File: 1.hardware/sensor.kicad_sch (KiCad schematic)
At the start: 13 parts, among them U10 Hall_Analog_Joystick, U2 LM75B, U9 Hall_Analog_Joystick

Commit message: 중간 저장
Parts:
- added C79, C80, C84, C88: 39nF/16V, symbol Device:C_Small_US
- added R125, R129, R2, R3: 100/0.1w, Resistor_SMD:R_0402_1005Metric, symbol Device:R_Small_US
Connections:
- net GND: now also C79.2, C80.2, C84.2, C88.2
- net Joystick1_H: now also C84.1, R125.1; no longer TP32.1, U9.2 (H)
- net Joystick1_V: now also C88.1, R129.2; no longer TP33.1, U9.5 (V)
- net Joystick2_H: now also C80.1, R3.1; no longer TP35.1, U10.2 (H)
- net Joystick2_V: now also C79.1, R2.2; no longer TP34.1, U10.5 (V)
- new net: R3.2, TP35.1, U10.2 (H)
- new net: R125.2, TP32.1, U9.2 (H)
- new net: R2.1, TP34.1, U10.5 (V)
- new net: R129.1, TP33.1, U9.5 (V)
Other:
- moved on the sheet: C67, R108, R109, R112, R113, R114, TP32, TP33, TP34, TP35, U10, U2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

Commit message: 핀 배치 완료
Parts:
- removed R113, R114: 10k/0.063w, Resistor_SMD:R_0402_1005Metric, symbol Device:R_Small_US
- removed U2: LM75B, symbol Sensor_Temperature:LM75B
- added RT1: NCP18XH103F03RB, THRMC1608X95N, symbol SamacSys_Parts:NCP18XH103F03RB
- R112: footprint Resistor_SMD:R_0402_1005Metric -> (none)
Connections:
- net +3.3V: no longer C67.1, R112.1
- net GND: now also R112.1
- net ADC_TEMP: now reaches R112.2
- net ADC_TEMP: now also C67.1, RT1.1
- new net ADC_VREF_2V5: RT1.2
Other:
- note removed: "TEMP"

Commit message: 중간 저장
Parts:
- C80: value 39nF/16V -> 39nF/50V; footprint (none) -> Capacitor_SMD:C_0402_1005Metric
- C81: renamed from C84; value 39nF/16V -> 39nF/50V; footprint (none) -> Capacitor_SMD:C_0402_1005Metric
- C82: renamed from C88; value 39nF/16V -> 39nF/50V; footprint (none) -> Capacitor_SMD:C_0402_1005Metric
- C83: renamed from C79; value 39nF/16V -> 39nF/50V; footprint (none) -> Capacitor_SMD:C_0402_1005Metric
- R131: renamed from R112; footprint (none) -> Resistor_SMD:R_0402_1005Metric
- R132: renamed from R3; footprint Resistor_SMD:R_0402_1005Metric -> Resistor_SMD:R_0603_1608Metric
- R133: renamed from R125; footprint Resistor_SMD:R_0402_1005Metric -> Resistor_SMD:R_0603_1608Metric
- R136: renamed from R129; footprint Resistor_SMD:R_0402_1005Metric -> Resistor_SMD:R_0603_1608Metric
- R137: renamed from R2; footprint Resistor_SMD:R_0402_1005Metric -> Resistor_SMD:R_0603_1608Metric
- TP10: renamed from TP33; footprint (none) -> TestPoint:TestPoint_Pad_D1.5mm
- TP11: renamed from TP34; footprint (none) -> TestPoint:TestPoint_Pad_D1.5mm
- TP8: renamed from TP35; footprint (none) -> TestPoint:TestPoint_Pad_D1.5mm
- TP9: renamed from TP32; footprint (none) -> TestPoint:TestPoint_Pad_D1.5mm
- renumbered C67 to C79, R108 to R134, R109 to R135, U9 to U7, U10 to U8

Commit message: 풋프린트 연결 완료
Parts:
- RT1: footprint THRMC1608X95N -> SamacSys_Parts_Project:THRMC1608X95N
- U7, U8: footprint New_Footprints:Hall_Analog_Joystick -> Library:Hall_Analog_Joystick
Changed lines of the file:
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@@
 			)
 		)
-		(property "Footprint" "New_Footprints:Hall_Analog_Joystick"
+		(property "Footprint" "Library:Hall_Analog_Joystick"
 			(at 95.25 120.65 0)
 			(effects
@@
 			)
 		)
-		(property "Footprint" "THRMC1608X95N"
+		(property "Footprint" "SamacSys_Parts_Project:THRMC1608X95N"
 			(at 55.88 175.26 0)
 			(effects
@@
 			)
 		)
-		(property "Footprint" "New_Footprints:Hall_Analog_Joystick"
+		(property "Footprint" "Library:Hall_Analog_Joystick"
 			(at 95.25 73.66 0)
 			(effects

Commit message: 중간 저장
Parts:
- removed C80, C83: 39nF/50V, Capacitor_SMD:C_0402_1005Metric, symbol Device:C_Small_US
- removed R132, R137: 100/0.1w, Resistor_SMD:R_0603_1608Metric, symbol Device:R_Small_US
- removed R135: 4.7k/0.063w, Resistor_SMD:R_0402_1005Metric, symbol Device:R_Small_US
- removed TP11: TP_JV2, TestPoint:TestPoint_Pad_D1.5mm, symbol Connector:TestPoint
- removed TP8: TP_JH2, TestPoint:TestPoint_Pad_D1.5mm, symbol Connector:TestPoint
- removed U8: Hall_Analog_Joystick, Library:Hall_Analog_Joystick, symbol New_Library:Hall_Analog_Sensor
- renumbered C79 to C81, C81 to C82, C82 to C83, R131 to R119, R133 to R120, R134 to R121, R136 to R122, TP9 to TP8, TP10 to TP9, U7 to U8
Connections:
- net Joystick1_H renamed Joystick_H
- net Joystick1_Sel renamed Joystick_Sel
- net Joystick1_V renamed Joystick_V

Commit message: 중간 저장
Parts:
- renumbered C82 to C81, C83 to C82, C81 to C83, R120 to R115, R122 to R116, R121 to R117, R119 to R118, TP8 to TP7, TP9 to TP8, U8 to U22
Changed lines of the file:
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@@
 		(dnp no)
 		(fields_autoplaced yes)
-		(property "Reference" "#PWR0121"
+		(property "Reference" "#PWR0114"
 			(at 102.87 95.25 0)
 			(effects
@@
 			(project "bldc_motor_controller"
 				(path "/a25adab6-a8c3-4e0e-8ba9-baac00aaa394/41a95291-f7f2-4bdf-b0a1-cf2084f10036"
-					(reference "#PWR0121")
+					(reference "#PWR0114")
 					(unit 1)
 				)
@@
 		(dnp no)
 		(fields_autoplaced yes)
-		(property "Reference" "#PWR0120"
+		(property "Reference" "#PWR0115"
 			(at 93.98 100.33 0)
 			(effects
@@
 			(project "bldc_motor_controller"
 				(path "/a25adab6-a8c3-4e0e-8ba9-baac00aaa394/41a95291-f7f2-4bdf-b0a1-cf2084f10036"
-					(reference "#PWR0120")
+					(reference "#PWR0115")
 					(unit 1)
 				)
@@
 		(on_board yes)
 		(dnp no)
-		(property "Reference" "R119"
+		(property "Reference" "R118"
 			(at 54.102 194.818 0)
 			(effects
@@
 			(project "bldc_motor_controller"
 				(path "/a25adab6-a8c3-4e0e-8ba9-baac00aaa394/41a95291-f7f2-4bdf-b0a1-cf2084f10036"
-					(reference "R119")
+					(reference "R118")
 					(unit 1)
 				)
@@
 		(dnp no)
 		(fields_autoplaced yes)
-		(property "Reference" "#PWR0119"
+		(property "Reference" "#PWR0112"
 			(at 60.96 90.17 0)
 			(effects
@@
 			(project "bldc_motor_controller"
 				(path "/a25adab6-a8c3-4e0e-8ba9-baac00aaa394/41a95291-f7f2-4bdf-b0a1-cf2084f10036"
-					(reference "#PWR0119")
+					(reference "#PWR0112")
 					(unit 1)
 				)
@@
 		(on_board yes)
 		(dnp no)
-		(property "Reference" "R120"
+		(property "Reference" "R115"
 			(at 65.532 71.374 90)
 			(effects
@@
 			(project "bldc_motor_controller"
 				(path "/a25adab6-a8c3-4e0e-8ba9-baac00aaa394/41a95291-f7f2-4bdf-b0a1-cf2084f10036"
-					(reference "R120")
+					(reference "R115")
 					(unit 1)
 				)
@@
 		(dnp no)
 		(fields_autoplaced yes)
-		(property "Reference" "#PWR0117"
+		(property "Reference" "#PWR0116"
 			(at 48.26 208.28 0)
 			(effects
@@
 			(project "bldc_motor_controller"
 				(path "/a25adab6-a8c3-4e0e-8ba9-baac00aaa394/41a95291-f7f2-4bdf-b0a1-cf2084f10036"
-					(reference "#PWR0117")
+					(reference "#PWR0116")
 					(unit 1)
 				)
@@
 		(on_board yes)
 		(dnp no)
-		(property "Reference" "TP8"
+		(property "Reference" "TP7"
 			(at 69.85 65.786 0)
 			(effects
@@
 			(project "bldc_motor_controller"
 				(path "/a25adab6-a8c3-4e0e-8ba9-baac00aaa394/41a95291-f7f2-4bdf-b0a1-cf2084f10036"
-					(reference "TP8")
+					(reference "TP7")
 					(unit 1)
 				)
@@
 		(on_board yes)
 		(dnp no)
-		(property "Reference" "C82"
+		(property "Reference" "C81"
 			(at 63.5 77.5969 0)
 			(effects
@@
 			(project "bldc_motor_controller"
 				(path "/a25adab6-a8c3-4e0e-8ba9-baac00aaa394/41a95291-f7f2-4bdf-b0a1-cf2084f10036"
-					(reference "C82")
+					(reference "C81")
 					(unit 1)
 				)
@@
 		(dnp no)
 		(fields_autoplaced yes)
-		(property "Reference" "#PWR0118"
+		(property "Reference" "#PWR0117"
 			(at 57.15 208.28 0)
 			(effects
@@
 			(project "bldc_motor_controller"
 				(path "/a25adab6-a8c3-4e0e-8ba9-baac00aaa394/41a95291-f7f2-4bdf-b0a1-cf2084f10036"
-					(reference "#PWR0118")
+					(reference "#PWR0117")
 					(unit 1)
 				)
@@
 		(dnp no)
 		(fields_autoplaced yes)
-		(property "Reference" "U8"
+		(property "Reference" "U22"
 			(at 95.885 62.23 0)
 			(effects
@@
 			(project ""
 				(path "/a25adab6-a8c3-4e0e-8ba9-baac00aaa394/41a95291-f7f2-4bdf-b0a1-cf2084f10036"
-					(reference "U8")
+					(reference "U22")
 					(unit 1)
 				)
@@
 		(on_board yes)
 		(dnp no)
-		(property "Reference" "R121"
+		(property "Reference" "R117"
 			(at 103.124 93.98 0)
 			(effects
@@
 			(project "bldc_motor_controller"
 				(path "/a25adab6-a8c3-4e0e-8ba9-baac00aaa394/41a95291-f7f2-4bdf-b0a1-cf2084f10036"
-					(reference "R121")
+					(reference "R117")
 					(unit 1)
 				)
@@
 		(on_board yes)
 		(dnp no)
-		(property "Reference" "C81"
+		(property "Reference" "C83"
 			(at 44.196 196.342 0)
 			(effects
@@
 			(project "bldc_motor_controller"
 				(path "/a25adab6-a8c3-4e0e-8ba9-baac00aaa394/41a95291-f7f2-4bdf-b0a1-cf2084f10036"
-					(reference "C81")
+					(reference "C83")
 					(unit 1)
 				)
@@
 		(dnp no)
 		(fields_autoplaced yes)
-		(property "Reference" "#PWR0122"
+		(property "Reference" "#PWR0113"
 			(at 130.81 90.17 0)
 			(effects
@@
 			(project "bldc_motor_controller"
 				(path "/a25adab6-a8c3-4e0e-8ba9-baac00aaa394/41a95291-f7f2-4bdf-b0a1-cf2084f10036"
-					(reference "#PWR0122")
+					(reference "#PWR0113")
 					(unit 1)
 				)
@@
 		(on_board yes)
 		(dnp no)
-		(property "Reference" "TP9"
+		(property "Reference" "TP8"
 			(at 115.57 65.278 0)
 			(effects
@@
 			(project "bldc_motor_controller"
 				(path "/a25adab6-a8c3-4e0e-8ba9-baac00aaa394/41a95291-f7f2-4bdf-b0a1-cf2084f10036"
-					(reference "TP9")
+					(reference "TP8")
 					(unit 1)
 				)
@@
 		(on_board yes)
 		(dnp no)
-		(property "Reference" "C83"
+		(property "Reference" "C82"
 			(at 133.35 77.5969 0)
 			(effects
@@
 			(project "bldc_motor_controller"
 				(path "/a25adab6-a8c3-4e0e-8ba9-baac00aaa394/41a95291-f7f2-4bdf-b0a1-cf2084f10036"
-					(reference "C83")
+					(reference "C82")
 					(unit 1)
 				)
@@
 		(on_board yes)
 		(dnp no)
-		(property "Reference" "R122"
+		(property "Reference" "R116"
 			(at 122.682 71.374 90)
 			(effects
@@
 			(project "bldc_motor_controller"
 				(path "/a25adab6-a8c3-4e0e-8ba9-baac00aaa394/41a95291-f7f2-4bdf-b0a1-cf2084f10036"
-					(reference "R122")
-					(unit 1)
-				)
+					(reference "R116")
+					(unit 1)
+				)

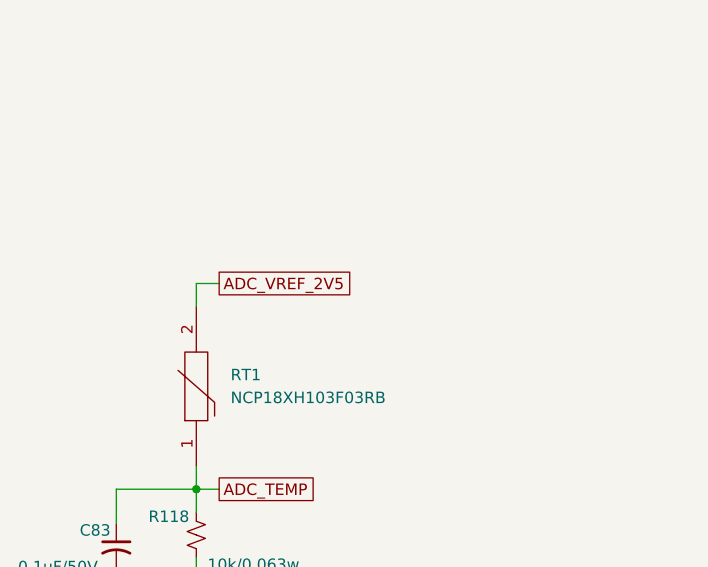
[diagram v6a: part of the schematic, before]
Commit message: 스펙 정함
4층 기판, 비아 0.3 / 0.5 사이즈, 외부 2온즈, Plugger Via, 77달러 정도 나옴
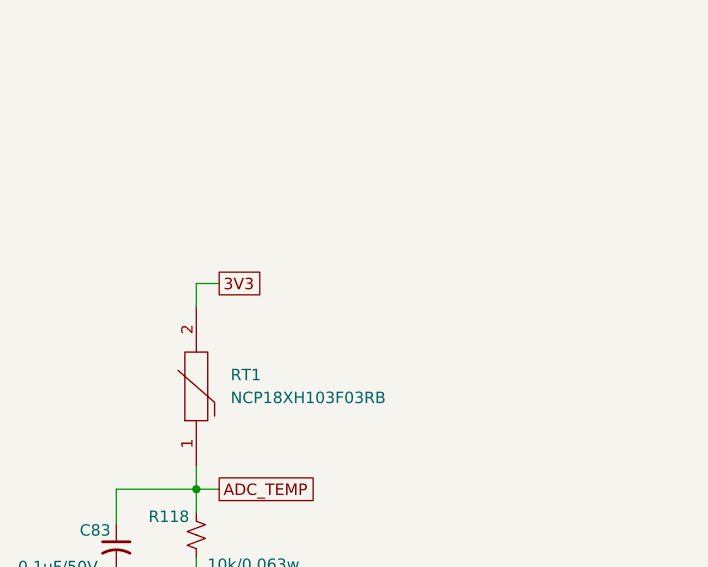
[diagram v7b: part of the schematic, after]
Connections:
- net ADC_VREF_2V5 renamed 3V3
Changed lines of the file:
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@@
 		)
 	)
-	(global_label "ADC_VREF_2V5"
+	(global_label "3V3"
 		(shape passive)
 		(at 59.69 168.91 0)
@@
 		)
 		(property "Intersheetrefs" "${INTERSHEET_REFS}"
-			(at 75.2315 168.91 0)
+			(at 65.0715 168.91 0)
 			(effects
 				(font

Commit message: 오류 일단 다 잡음
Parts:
- C83: footprint Capacitor_SMD:C_0603_1608Metric -> Capacitor_SMD:C_0402_1005Metric
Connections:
- net +3.3V is gone; now on net 3V3: R117.1
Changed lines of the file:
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@@
+		)
+	)
+	(global_label "3V3"
+		(shape passive)
+		(at 102.87 91.44 0)
+		(fields_autoplaced yes)
+		(effects
+			(font
+				(size 1.27 1.27)
+			)
+			(justify left)
+		)
+		(property "Intersheetrefs" "${INTERSHEET_REFS}"
+			(at 108.2515 91.44 0)
+			(effects
+				(font
+					(size 1.27 1.27)
+				)
+				(justify left)
+				(hide yes)
+			)
 		)
 	)
@@
 	)
 	(symbol
-		(lib_id "power:+3.3V")
-		(at 102.87 91.44 0)
-		(unit 1)
-		(exclude_from_sim no)
-		(in_bom yes)
-		(on_board yes)
-		(dnp no)
-		(fields_autoplaced yes)
-		(property "Reference" "#PWR0114"
-			(at 102.87 95.25 0)
-			(effects
-				(font
-					(size 1.27 1.27)
-				)
-				(hide yes)
-			)
-		)
-		(property "Value" "+3.3V"
-			(at 102.87 86.36 0)
-			(effects
-				(font
-					(size 1.27 1.27)
-				)
-			)
-		)
-		(property "Footprint" ""
-			(at 102.87 91.44 0)
-			(effects
-				(font
-					(size 1.27 1.27)
-				)
-				(hide yes)
-			)
-		)
-		(property "Datasheet" ""
-			(at 102.87 91.44 0)
-			(effects
-				(font
-					(size 1.27 1.27)
-				)
-				(hide yes)
-			)
-		)
-		(property "Description" "Power symbol creates a global label with name \"+3.3V\""
-			(at 102.87 91.44 0)
-			(effects
-				(font
-					(size 1.27 1.27)
-				)
-				(hide yes)
-			)
-		)
-		(pin "1"
-		)
-		(instances
-			(project "bldc_motor_controller"
-				(path "/a25adab6-a8c3-4e0e-8ba9-baac00aaa394/41a95291-f7f2-4bdf-b0a1-cf2084f10036"
-					(reference "#PWR0114")
-					(unit 1)
-				)
-			)
-		)
-	)
-	(symbol
 		(lib_id "power:GND")
 		(at 93.98 93.98 0)
@@
 			)
 		)
-		(property "Footprint" "Capacitor_SMD:C_0603_1608Metric"
+		(property "Footprint" "Capacitor_SMD:C_0402_1005Metric"
 			(at 48.26 198.12 0)
 			(effects
